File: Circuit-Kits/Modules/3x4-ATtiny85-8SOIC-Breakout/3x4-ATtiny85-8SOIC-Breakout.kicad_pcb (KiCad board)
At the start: 2 copper layers, 0 parts

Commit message: Add ATtiny85, 555 Timer pads. Silk looks awful.
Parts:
- added REF**: 8DIP IC, Crazy_Circuits:DIP8-3x4, F.Cu at (192.5, 61.1)
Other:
- board outline added: 23.6 x 31.6 mm
- board text added: "FABRICATION NOTES 1. THIS IS A 2 LAYER BOARD. 2. EXTERNAL LAYERS SHALL HAVE 1 OZ COPPER. 3. MATERIAL: FR4 AND 0.062 INCH +/- 10% THICK. 4. BOARDS SHALL BE ROHS COMPLIANT. 5. MANUFACTURE IN ACCORDANCE WITH IPC-6012 CLASS 2 6. MASK: BOTH SIDES OF THE BOARD SHALL HAVE SOLDER MASK (GREEN) OVER BARE COPPER. 7. SILK: BOTH SIDES OF THE BOARD SHALL HAVE WHITE SILKSCREEN. DO NOT PLACE SILK OVER BARE COPPE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"
- board text removed: "FABRICATION NOTES 1. THIS IS A 2 LAYER BOARD. 2. EXTERNAL LAYERS SHALL HAVE 1 OZ COPPER. 3. MATERIAL: FR4 AND 0.062 INCH +/- 10% THICK. 4. BOARDS SHALL BE ROHS COMPLIANT. 5. MANUFACTURE IN ACCORDANCE WITH IPC-6012 CLASS 2 6. MASK: BOTH SIDES OF THE BOARD SHALL HAVE SOLDER MASK (ANY COLOR) OVER BARE COPPER. 7. SILK: BOTH SIDES OF THE BOARD SHALL HAVE WHITE SILKSCREEN. DO NOT PLACE SILK OVER BARE C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"

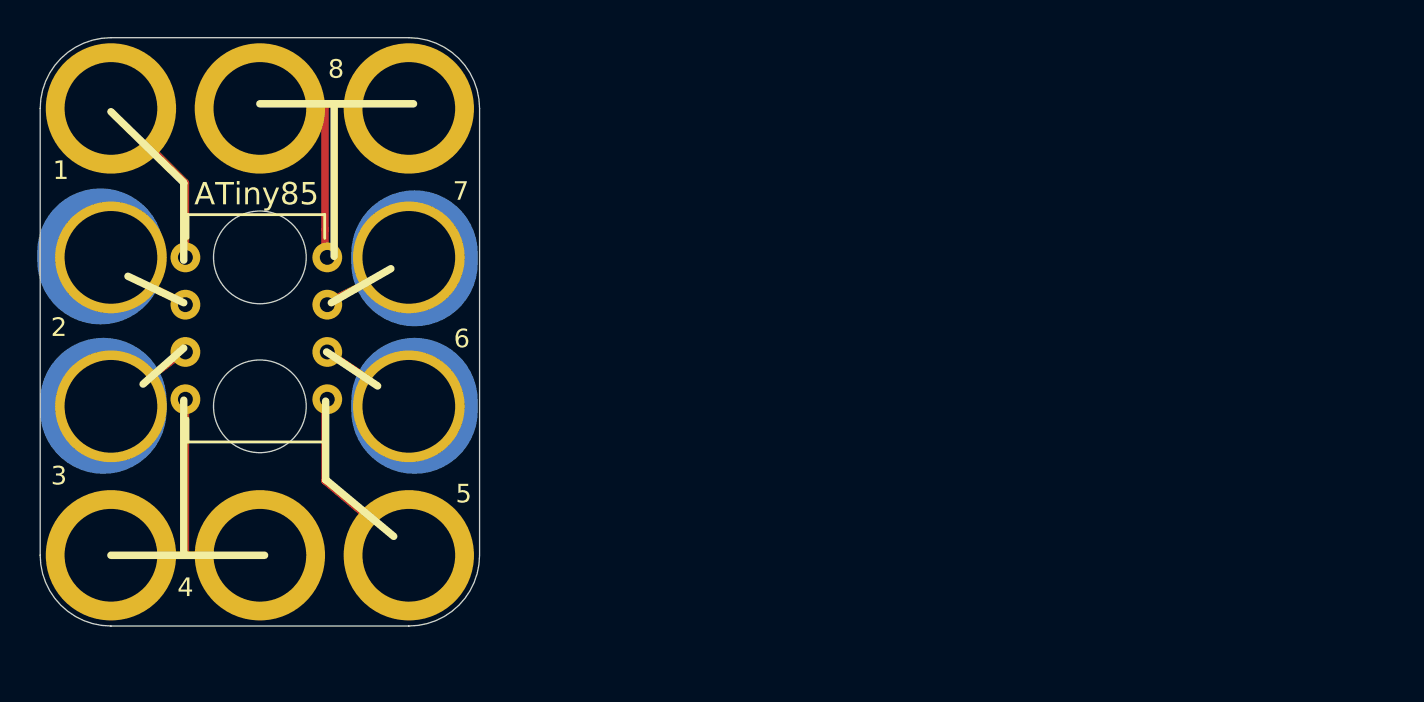
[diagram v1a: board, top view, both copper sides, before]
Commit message: Add license. Removed two from module page.
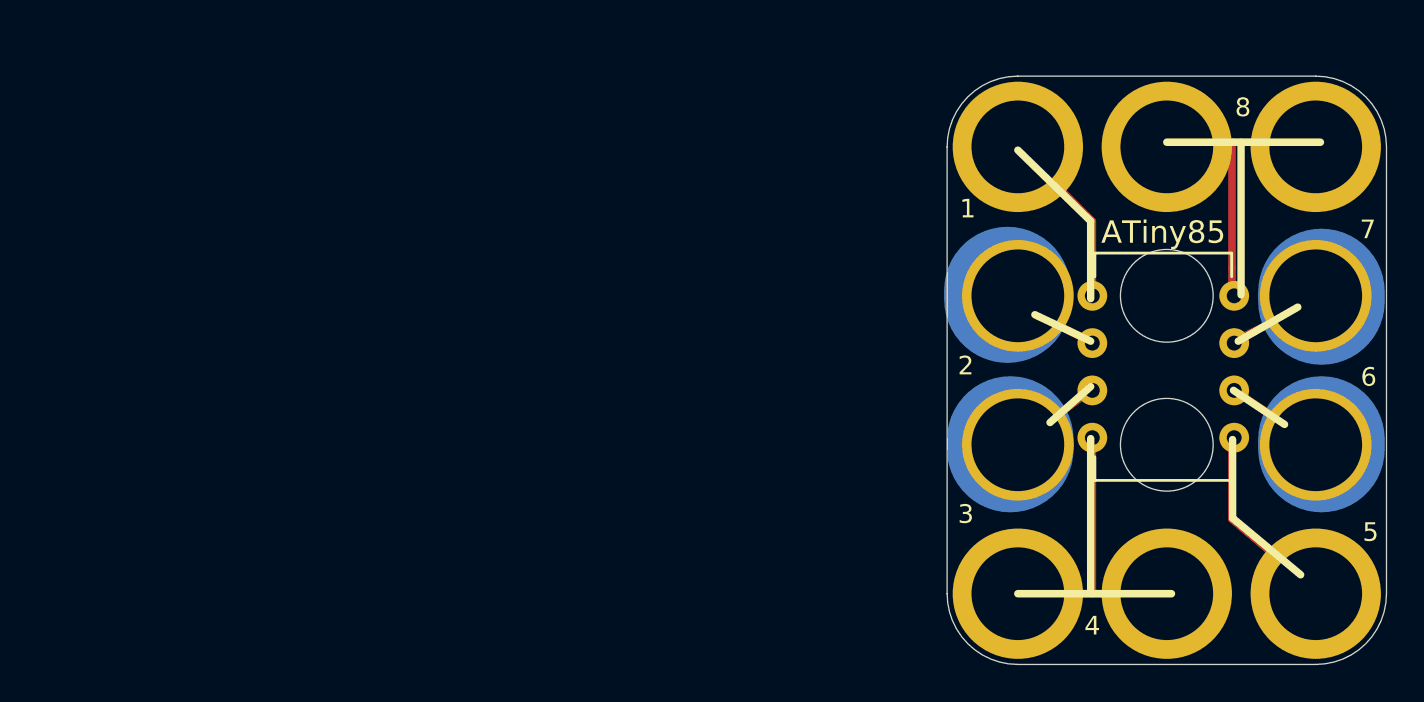
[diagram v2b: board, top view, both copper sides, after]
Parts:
- moved REF** 48.8 mm to (241.2, 63.1)
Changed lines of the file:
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@@
     (links 0)
     (no_connects 0)
-    (area 120.3198 33.909 263.164559 102.997)
+    (area 120.3198 32.987679 263.164559 102.997)
     (thickness 1.6)
     (drawings 1)
@@
   )
   (module Crazy_Circuits:DIP8-3x4 (layer F.Cu)
-    (at 192.49644 61.06668)
+    (at 241.20956 63.13124)
     (descr "8-lead dip package, row spacing 7.62 mm (300 mils)")
     (tags "dil dip 2.54 300")
@@
     (pad 7 thru_hole oval (at 11.62 -13.46) (size 1.6 1.6) (drill 0.8) (layers *.Cu *.Mask F.SilkS))
     (pad 8 thru_hole oval (at 11.62 -16) (size 1.6 1.6) (drill 0.8) (layers *.Cu *.Mask F.SilkS))
-    (pad 4 thru_hole circle (at 0 0 270) (size 7 7) (drill 4.98) (layers *.Cu *.Mask))
-    (pad "" np_thru_hole circle (at 8 -16 270) (size 4.98 4.98) (drill 4.98) (layers *.Cu *.Mask))
-    (pad 2 thru_hole circle (at 0 -16 270) (size 6 6) (drill 4.98) (layers *.Cu *.Mask))
-    (pad 3 thru_hole circle (at 0 -8 270) (size 6 6) (drill 4.98) (layers *.Cu *.Mask))
-    (pad "" np_thru_hole circle (at 8 -8 270) (size 4.98 4.98) (drill 4.98) (layers *.Cu *.Mask F.SilkS))
-    (pad 4 thru_hole circle (at 8 0 270) (size 7 7) (drill 4.98) (layers *.Cu *.Mask))
-    (pad 1 thru_hole circle (at 0 -24 270) (size 7 7) (drill 4.98) (layers *.Cu *.Mask))
-    (pad 7 thru_hole circle (at 16 -16 270) (size 6 6) (drill 4.98) (layers *.Cu *.Mask))
-    (pad 5 thru_hole circle (at 16 0 270) (size 7 7) (drill 4.98) (layers *.Cu *.Mask))
-    (pad 6 thru_hole circle (at 16 -8 270) (size 6 6) (drill 4.98) (layers *.Cu *.Mask))
-    (pad 8 thru_hole circle (at 16 -24 270) (size 7 7) (drill 4.98) (layers *.Cu *.Mask))
-    (pad 8 thru_hole circle (at 8 -24 270) (size 7 7) (drill 4.98) (layers *.Cu *.Mask))
+    (pad 4 thru_hole circle (at 0 0 270) (size 7 7) (drill 4.98) (layers *.Cu B.Mask))
+    (pad "" np_thru_hole circle (at 8 -16 270) (size 4.98 4.98) (drill 4.98) (layers *.Cu B.Mask))
+    (pad 2 thru_hole circle (at 0 -16 270) (size 6 6) (drill 4.98) (layers *.Cu B.Mask))
+    (pad 3 thru_hole circle (at 0 -8 270) (size 6 6) (drill 4.98) (layers *.Cu B.Mask))
+    (pad "" np_thru_hole circle (at 8 -8 270) (size 4.98 4.98) (drill 4.98) (layers *.Cu B.Mask F.SilkS))
+    (pad 4 thru_hole circle (at 8 0 270) (size 7 7) (drill 4.98) (layers *.Cu B.Mask))
+    (pad 1 thru_hole circle (at 0 -24 270) (size 7 7) (drill 4.98) (layers *.Cu B.Mask))
+    (pad 7 thru_hole circle (at 16 -16 270) (size 6 6) (drill 4.98) (layers *.Cu B.Mask))
+    (pad 5 thru_hole circle (at 16 0 270) (size 7 7) (drill 4.98) (layers *.Cu B.Mask))
+    (pad 6 thru_hole circle (at 16 -8 270) (size 6 6) (drill 4.98) (layers *.Cu B.Mask))
+    (pad 8 thru_hole circle (at 16 -24 270) (size 7 7) (drill 4.98) (layers *.Cu B.Mask))
+    (pad 8 thru_hole circle (at 8 -24 270) (size 7 7) (drill 4.98) (layers *.Cu B.Mask))
     (model Housings_DIP.3dshapes/DIP-8_W7.62mm.wrl
       (at (xyz 0 0 0))

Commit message: Add 3x4 ATtiny85 v1.0
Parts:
- removed REF**: 8DIP IC, Crazy_Circuits:DIP8-3x4
- added U1: ATTINY85-8SOIC, Crazy_Circuits:SOIC8-ATtiny85-3x4, F.Cu at (5.18, 65.1)
